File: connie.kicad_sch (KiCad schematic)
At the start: 143 parts, among them J1 Conn_01x03, J2 Conn_01x02, J3 Conn_01x02, J4 Conn_01x03, J5 Barrel_Jack_Switch, Q1 DTC143Z, Q2 DTC143Z, Q3 DTC143Z, Q4 DTC143Z, SW1 DIP_1188E, SW2 DIP_1188E, SW3 DIP_1188E, SW4 DIP_1188E, SW5 DIP_1188E, U1 emmc_bga153, U3 ES8388, U4 CS8676E, U5 74LVC1G02, U6 MAX803, U7 MAX803, U8 74LVC1G02, U9 TPS562200

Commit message: add c3 module
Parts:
- removed J1: Conn_01x03, Connector_PinHeader_2.54mm:PinHeader_1x03_P2.54mm_Vertical, symbol Connector_Generic:Conn_01x03
- added C100: 22u, Capacitor_SMD:C_1206_3216Metric, symbol Device:C
- added C101, C102: 0.1u, Capacitor_SMD:C_0603_1608Metric, symbol Device:C
- added J1: Conn_01x05, Connector_PinHeader_2.54mm:PinHeader_1x05_P2.54mm_Vertical, symbol Connector_Generic:Conn_01x05
- added R100, R101: 1k, Resistor_SMD:R_0603_1608Metric, symbol Device:R
- added R103, R104: 10k, Resistor_SMD:R_0603_1608Metric, symbol Device:R
- added U10: ESP32-C3-mini-1, Espressif:ESP32-C3-MINI-1, symbol connie-lib:c
- C15, C22, C23, C24: footprint Capacitor_SMD:C_0805_2012Metric -> Capacitor_SMD:C_0603_1608Metric
- R26, R27, R28, R31, R32, R33, R42, R43: value R -> 10k
- U2: value (none) -> ESP32_WROVER; footprint (none) -> Espressif:ESP32-WROVER-E_Thermal_Vias
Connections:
- net +3V3: now also R35.2, C100.2, C101.1, R103.1, R104.1, U10.3 (3V3); no longer R35.1
- net EN: now also C102.2, U10.8 (EN/CHIP_PU)
- net GND: now also C37.1, C100.1, C101.2, C102.1, J1.3 (Pin_3), J1.4 (Pin_4), U10.1 (GND), U10.11 (GND), U10.14 (GND), U10.2 (GND), U10.36 (GND); no longer C37.2
- net MODE: now also C37.2; no longer C37.1
- net OUTNL2: now also J3.1 (Pin_1); no longer J3.2 (Pin_2)
- net OUTNR2: now also J2.2 (Pin_2); no longer J2.1 (Pin_1)
- net OUTPL2: now also J3.2 (Pin_2); no longer J3.1 (Pin_1)
- net OUTPR2: now also J2.1 (Pin_1); no longer J2.2 (Pin_2)
- net PLAY: now also R35.1; no longer R35.2
- net RXD1: now also R101.1
- net TXD1: now also R100.1
- new net: R104.2, U10.22 (GPIO8)
- new net: R103.2, U10.5 (GPIO2/ADC1_CH2)
- new net: J1.5 (Pin_5), U10.23 (GPIO9)
- new net C3_RXD0: J1.2 (Pin_2), U10.30 (GPIO20/U0RXD)
- new net C3_RXD1: R100.2, U10.20 (GPIO6)
- new net C3_TXD0: J1.1 (Pin_1), U10.31 (GPIO21/U0TXD)
- new net C3_TXD1: R101.2, U10.21 (GPIO7)
- no-connect marks 18 -> 26
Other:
- moved on the sheet: C15, C22, C23, C24, C30, C31, C32, C33, C34, C35, C36, C37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

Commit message: prepare to rename refs
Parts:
- renumbered R2 to R1, R3 to R2, R4 to R3, R1 to R4
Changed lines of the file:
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@@
   (symbol (lib_id "Device:R") (at 21.59 160.02 90) (unit 1)
     (in_bom yes) (on_board yes)
-    (property "Reference" "R3" (id 0) (at 26.67 158.75 90))
+    (property "Reference" "R2" (id 0) (at 26.67 158.75 90))
     (property "Value" "33" (id 1) (at 21.59 160.02 90))
     (property "Footprint" "Resistor_SMD:R_0603_1608Metric" (id 2) (at 21.59 161.798 90)
@@
   (symbol (lib_id "Device:R") (at 21.59 165.1 90) (unit 1)
     (in_bom yes) (on_board yes)
-    (property "Reference" "R1" (id 0) (at 26.67 163.83 90))
+    (property "Reference" "R4" (id 0) (at 26.67 163.83 90))
     (property "Value" "33" (id 1) (at 21.59 165.1 90))
     (property "Footprint" "Resistor_SMD:R_0603_1608Metric" (id 2) (at 21.59 166.878 90)
@@
   (symbol (lib_id "Device:R") (at 21.59 157.48 90) (unit 1)
     (in_bom yes) (on_board yes)
-    (property "Reference" "R4" (id 0) (at 26.67 156.21 90))
+    (property "Reference" "R3" (id 0) (at 26.67 156.21 90))
     (property "Value" "33" (id 1) (at 21.59 157.48 90))
     (property "Footprint" "Resistor_SMD:R_0603_1608Metric" (id 2) (at 21.59 159.258 90)
@@
   (symbol (lib_id "Device:R") (at 21.59 162.56 90) (unit 1)
     (in_bom yes) (on_board yes)
-    (property "Reference" "R2" (id 0) (at 26.67 161.29 90))
+    (property "Reference" "R1" (id 0) (at 26.67 161.29 90))
     (property "Value" "33" (id 1) (at 21.59 162.56 90))
     (property "Footprint" "Resistor_SMD:R_0603_1608Metric" (id 2) (at 21.59 164.338 90)
@@
       (reference "Q4") (unit 1) (value "DTC143Z") (footprint "Package_TO_SOT_SMD:SOT-23")
     )
+    (path "/f95bf3a5-5302-41d3-a2db-2263542d0696"
+      (reference "R1") (unit 1) (value "33") (footprint "Resistor_SMD:R_0603_1608Metric")
+    )
+    (path "/94a054e2-bafe-477a-a6c6-a1ed40dff911"
+      (reference "R2") (unit 1) (value "33") (footprint "Resistor_SMD:R_0603_1608Metric")
+    )
+    (path "/ecc35952-8ff0-49f7-939a-ee69c7eb30f7"
+      (reference "R3") (unit 1) (value "33") (footprint "Resistor_SMD:R_0603_1608Metric")
+    )
     (path "/a95cdc4d-00a4-4bf0-80f3-df5d0747d5a0"
-      (reference "R1") (unit 1) (value "33") (footprint "Resistor_SMD:R_0603_1608Metric")
-    )
-    (path "/f95bf3a5-5302-41d3-a2db-2263542d0696"
-      (reference "R2") (unit 1) (value "33") (footprint "Resistor_SMD:R_0603_1608Metric")
-    )
-    (path "/94a054e2-bafe-477a-a6c6-a1ed40dff911"
-      (reference "R3") (unit 1) (value "33") (footprint "Resistor_SMD:R_0603_1608Metric")
-    )
-    (path "/ecc35952-8ff0-49f7-939a-ee69c7eb30f7"
       (reference "R4") (unit 1) (value "33") (footprint "Resistor_SMD:R_0603_1608Metric")
     )

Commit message: reannotate resistors
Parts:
- renumbered R8 to R10, R9 to R11, R15 to R12, R7 to R13, R10 to R14, R12 to R15, R100 to R16, R101 to R17, R14 to R18, R17 to R19, R16 to R20, R19 to R21, R20 to R22, R21 to R23, R23 to R24, R22 to R25, R24 to R26, R25 to R27, R103 to R28, R104 to R29, R28 to R30, R33 to R32, R27 to R33, R26 to R34, R32 to R35, R43 to R36, R42 to R37, R34 to R38, R35 to R39, R36 to R40, R30 to R41, R29 to R42, R44 to R43, R37 to R44, R38 to R45, R40 to R46, R39 to R47, R41 to R48, R48 to R49, R6 to R5, R45 to R50, R46 to R51, R47 to R52, R18 to R6, R13 to R7, R5 to R8, R11 to R9

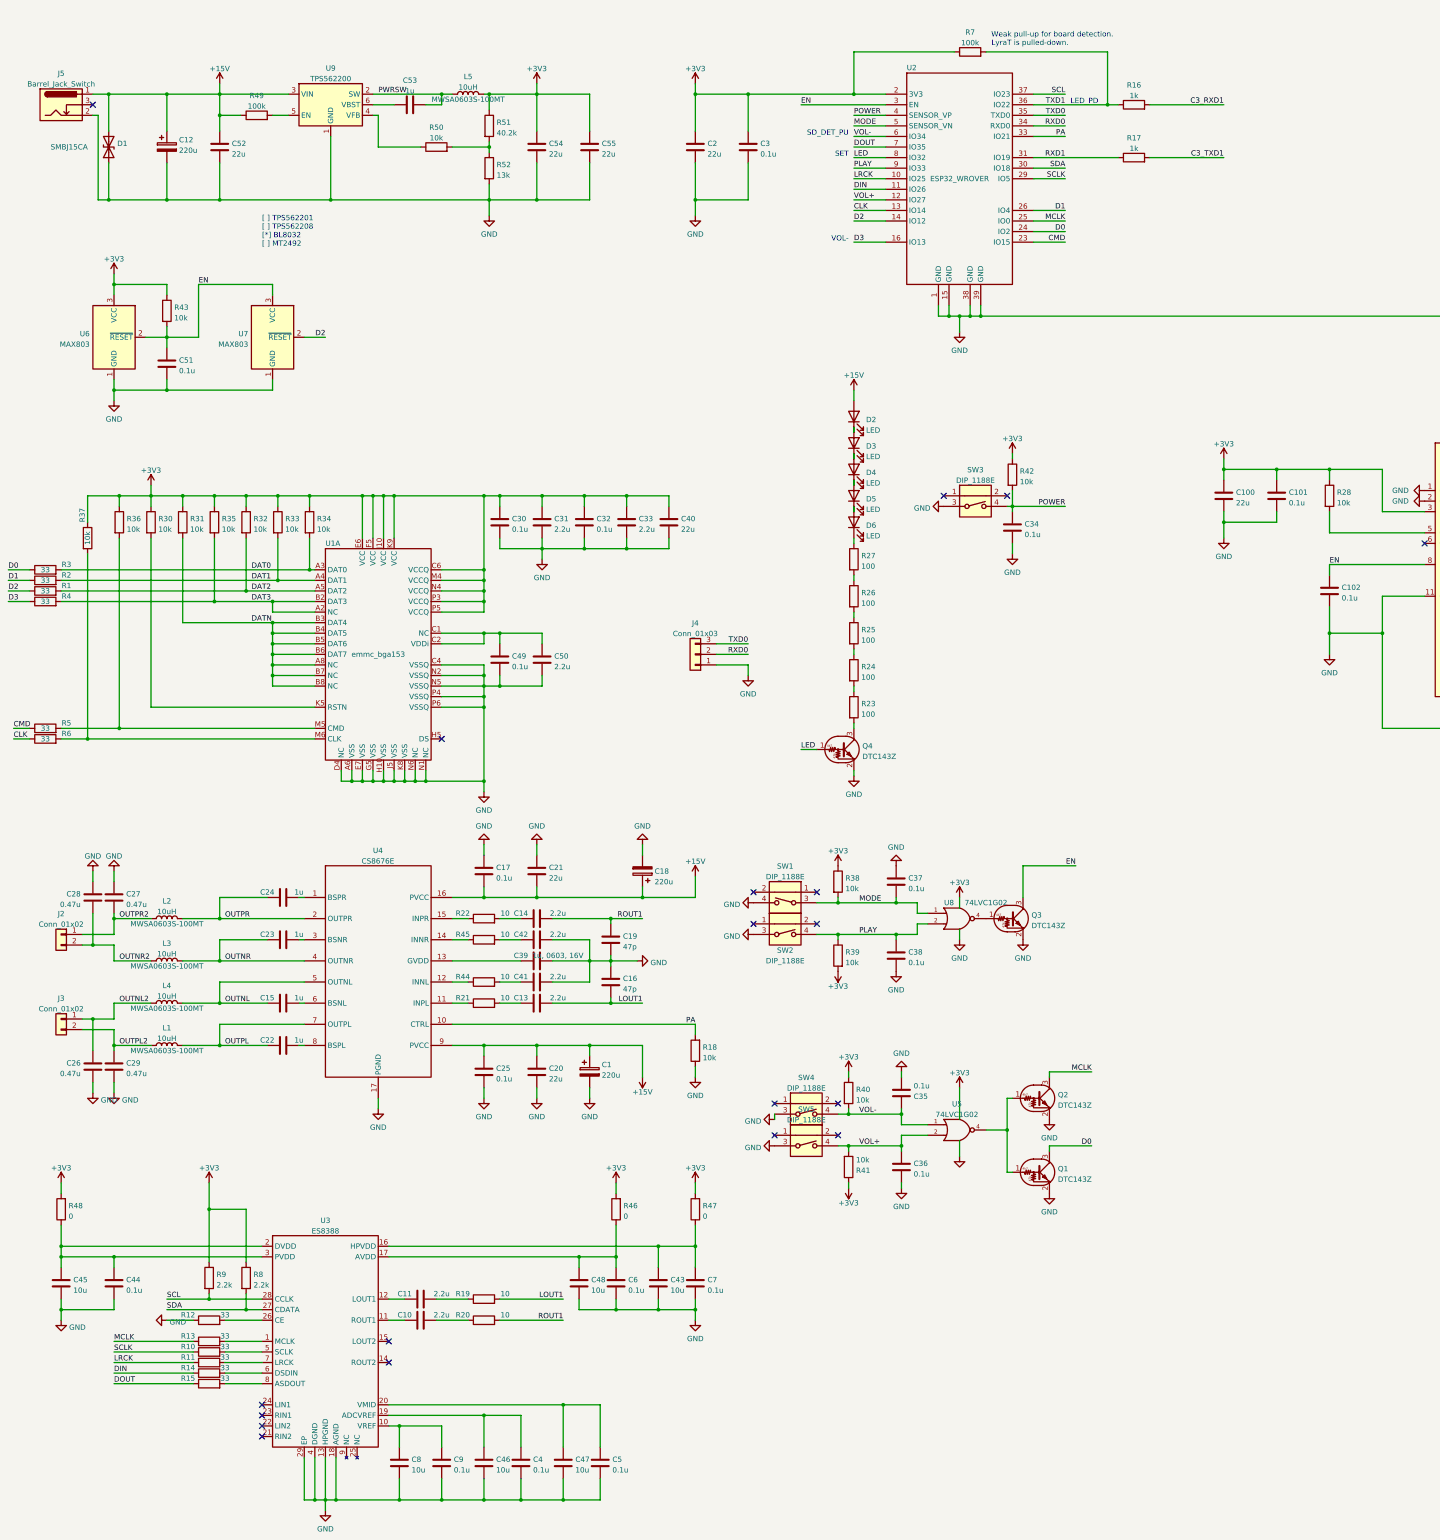
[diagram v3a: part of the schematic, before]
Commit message: reannotate caps
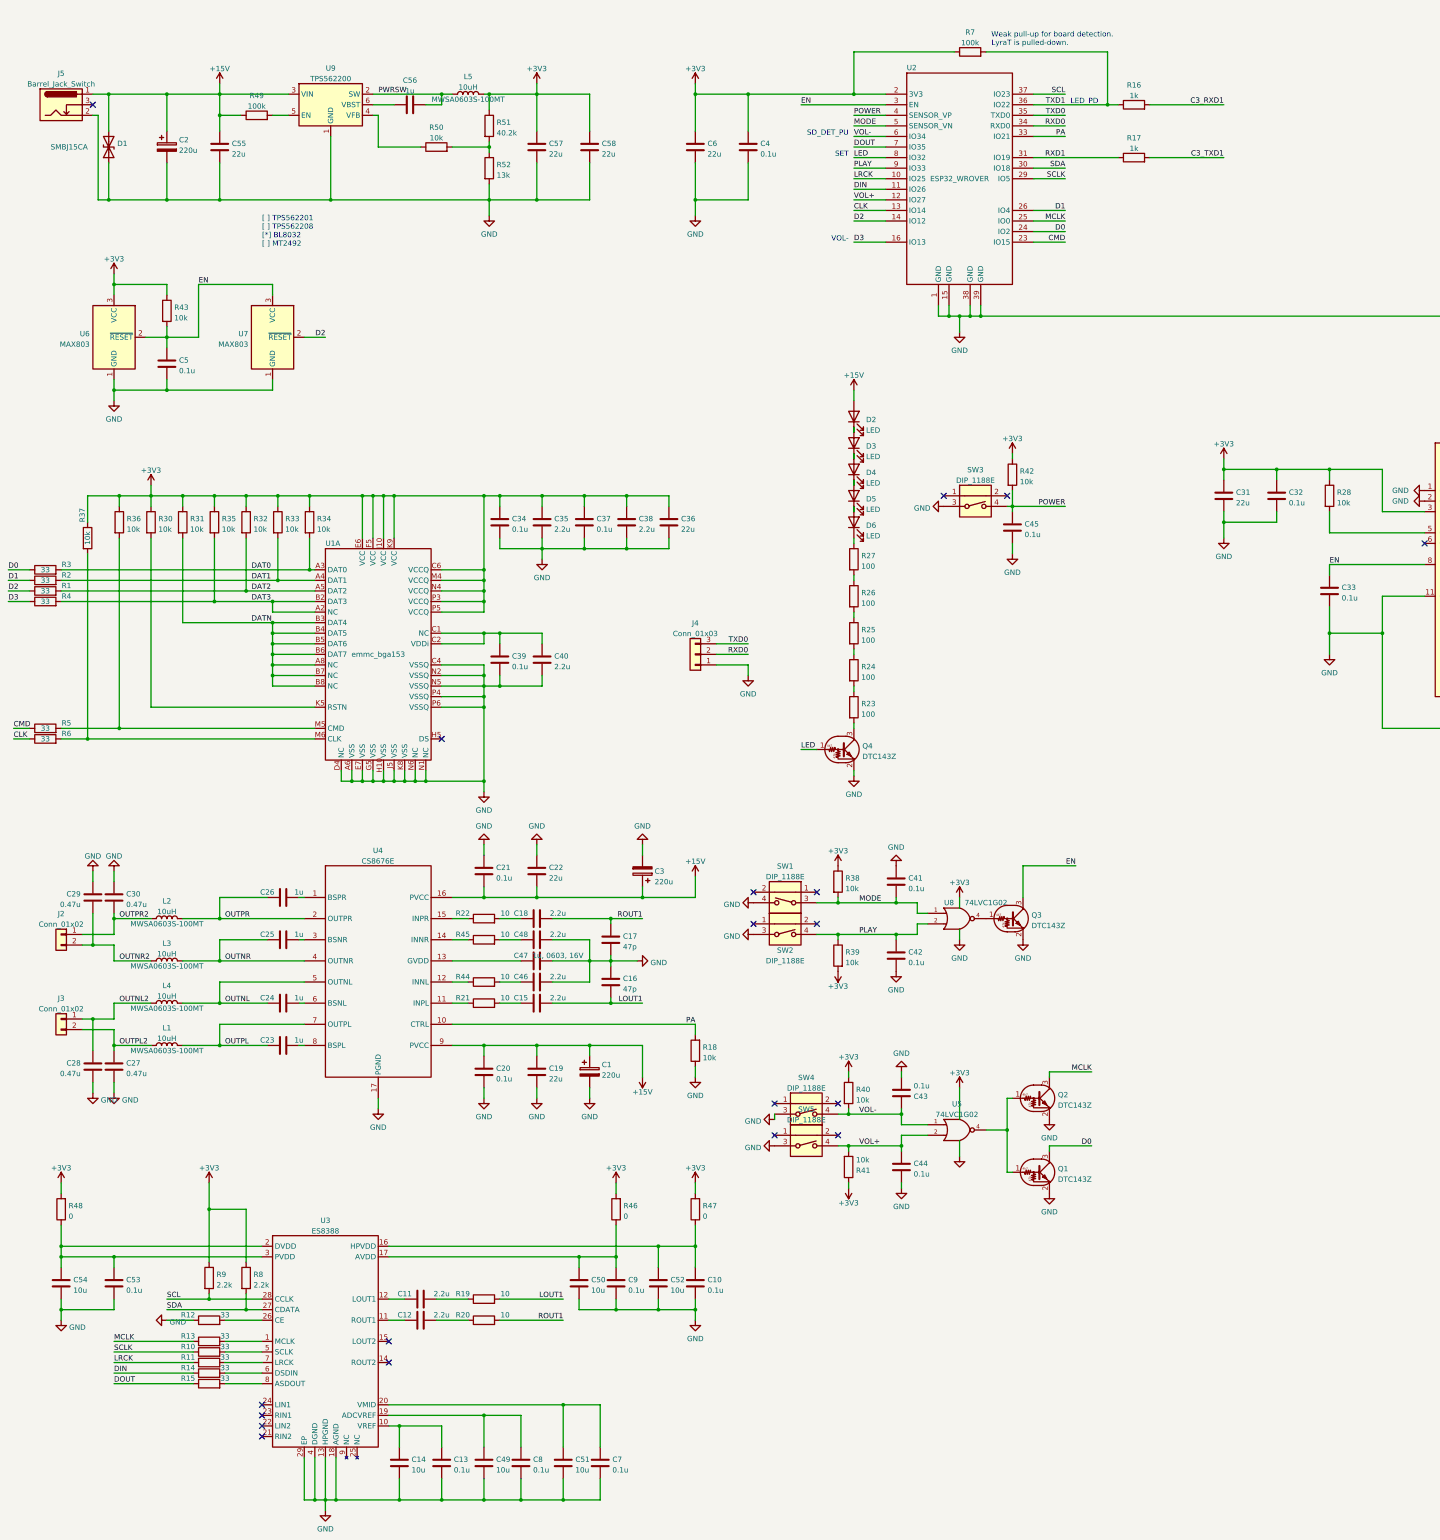
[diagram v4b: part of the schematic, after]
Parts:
- renumbered C7 to C10, C10 to C12, C9 to C13, C8 to C14, C13 to C15, C19 to C17, C14 to C18, C20 to C19, C12 to C2, C25 to C20, C17 to C21, C21 to C22, C22 to C23, C15 to C24, C23 to C25, C24 to C26, C29 to C27, C26 to C28, C28 to C29, C18 to C3, C27 to C30, C100 to C31, C101 to C32, C102 to C33, C30 to C34, C31 to C35, C40 to C36, C32 to C37, C33 to C38, C49 to C39, C3 to C4, C50 to C40, C37 to C41, C38 to C42, C35 to C43, C36 to C44, C34 to C45, C41 to C46, C39 to C47, C42 to C48, C46 to C49, C51 to C5, C48 to C50, C47 to C51, C43 to C52, C44 to C53, C45 to C54, C52 to C55, C53 to C56, C54 to C57, C55 to C58, C2 to C6, C5 to C7, C4 to C8, C6 to C9

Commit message: prepare for manufacturing
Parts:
- removed U10: ESP32-C3-mini-1, Espressif:ESP32-C3-MINI-1, symbol connie-lib:c
- added FID1, FID2, FID3, FID4, FID5, FID6: (no value), symbol Mechanical:Fiducial
- added TP1, TP10, TP11, TP12, TP13, TP2, TP3, TP4, TP5, TP6, TP7: (no value), symbol Connector:TestPoint
- added U5: (no value), symbol connie-lib:ESP32-C3-MINI-1
- C1, C2, C3: value 220u -> (none); footprint Capacitor_SMD:CP_Elec_8x10.5 -> (none)
- C10, C13, C32, C33, C34, C37, C39, C4, C41, C42, C43, C44, C45, C5, C53, C7, C8, C9: value 0.1u -> (none); footprint Capacitor_SMD:C_0603_1608Metric -> (none)
- C11, C12, C15, C18, C35, C38, C40, C46, C48: value 2.2u -> (none); footprint Capacitor_SMD:C_0603_1608Metric -> (none)
- C14, C49, C50, C51, C52, C54: value 10u -> (none); footprint Capacitor_SMD:C_0805_2012Metric -> (none)
- C16, C17: value 47p -> (none); footprint Capacitor_SMD:C_0603_1608Metric -> (none)
- C19, C22, C31, C36, C55, C57, C58, C6: value 22u -> (none); footprint Capacitor_SMD:C_1206_3216Metric -> (none)
- C20, C21: value 0.1u -> (none); footprint Capacitor_SMD:C_0805_2012Metric -> (none)
- C23, C24, C25, C26, C56: value 1u -> (none); footprint Capacitor_SMD:C_0603_1608Metric -> (none)
- C27, C28, C29, C30: value 0.47u -> (none); footprint Capacitor_SMD:C_0805_2012Metric -> (none)
- C47: value 1u, 0603, 16V -> (none); footprint Capacitor_SMD:C_0603_1608Metric -> (none)
- D1: value SMBJ15CA -> (none); footprint Diode_SMD:D_SMB -> (none)
- D2, D3, D4, D5, D6: value LED -> (none); footprint LED_SMD:LED_0603_1608Metric -> (none)
- H1, H2, H3, H5: value MountingHole -> (none); footprint Library:MountingHole_2.8mm_M2.5 -> (none)
- H4, H6: value MountingHole -> (none); footprint Library:MountingHole_1.7mm -> (none)
- J1: renamed from J3; value Conn_01x02 -> (none); footprint Connector_JST:JST_PH_B2B-PH-K_1x02_P2.00mm_Vertical -> (none)
- J2: value Conn_01x02 -> (none); footprint Connector_JST:JST_PH_B2B-PH-K_1x02_P2.00mm_Vertical -> (none)
- J3: renamed from J1; value Conn_01x05 -> (none); footprint Connector_PinHeader_2.54mm:PinHeader_1x05_P2.54mm_Vertical -> (none)
- J4: value Conn_01x03 -> (none); footprint Connector_PinHeader_2.54mm:PinHeader_1x03_P2.54mm_Vertical -> (none)
- J5: value Barrel_Jack_Switch -> (none); footprint Library:69410X402002 -> (none)
- L1, L3, L5: value 10uH -> (none); footprint Library:Sunlord_MWSA0603_6.6x7.1_H3.0 -> (none)
- L2: renamed from L4; value 10uH -> (none); footprint Library:Sunlord_MWSA0603_6.6x7.1_H3.0 -> (none)
- L4: renamed from L2; value 10uH -> (none); footprint Library:Sunlord_MWSA0603_6.6x7.1_H3.0 -> (none)
- Q1: renamed from Q4; value DTC143Z -> (none); footprint Package_TO_SOT_SMD:SOT-23 -> (none)
- Q2: renamed from Q1; value DTC143Z -> (none); footprint Package_TO_SOT_SMD:SOT-23 -> (none)
- Q3: renamed from Q2; value DTC143Z -> (none); footprint Package_TO_SOT_SMD:SOT-23 -> (none)
- Q4: renamed from Q3; value DTC143Z -> (none); footprint Package_TO_SOT_SMD:SOT-23 -> (none)
- R1, R10, R11, R12, R13, R14, R15, R2, R3, R4, R5, R6: value 33 -> (none); footprint Resistor_SMD:R_0603_1608Metric -> (none)
- R16, R17: value 1k -> (none); footprint Resistor_SMD:R_0603_1608Metric -> (none)
- R18, R28, R29, R30, R31, R32, R33, R34, R35, R36, R37, R38, R39, R40, R41, R42, R43, R50: value 10k -> (none); footprint Resistor_SMD:R_0603_1608Metric -> (none)
- R19, R20, R21, R22, R44, R45: value 10 -> (none); footprint Resistor_SMD:R_0603_1608Metric -> (none)
- R23, R24, R25, R26, R27: value 100 -> (none); footprint Resistor_SMD:R_0603_1608Metric -> (none)
- R46, R47, R48: value 0 -> (none); footprint Resistor_SMD:R_0603_1608Metric -> (none)
- R49, R7: value 100k -> (none); footprint Resistor_SMD:R_0603_1608Metric -> (none)
- R51: value 40.2k -> (none); footprint Resistor_SMD:R_0603_1608Metric -> (none)
- R52: value 13k -> (none); footprint Resistor_SMD:R_0603_1608Metric -> (none)
- R8, R9: value 2.2k -> (none); footprint Resistor_SMD:R_0603_1608Metric -> (none)
- SW1: renamed from SW5; value DIP_1188E -> (none); footprint Library:DIP_1188E -> (none); symbol connie-lib:DIP_1188E -> Connie:DIP1188E
- SW2: renamed from SW4; value DIP_1188E -> (none); footprint Library:DIP_1188E -> (none); symbol connie-lib:DIP_1188E -> Connie:DIP1188E
- SW3: value DIP_1188E -> (none); footprint Library:DIP_1188E -> (none); symbol connie-lib:DIP_1188E -> Connie:DIP1188E
- SW4: renamed from SW2; value DIP_1188E -> (none); footprint Library:DIP_1188E -> (none); symbol connie-lib:DIP_1188E -> Connie:DIP1188E
- SW5: renamed from SW1; value DIP_1188E -> (none); footprint Library:DIP_1188E -> (none); symbol connie-lib:DIP_1188E -> Connie:DIP1188E
- U1: renamed from U2; value ESP32_WROVER -> (none); footprint Espressif:ESP32-WROVER-E_Thermal_Vias -> (none); symbol connie-lib:ESP32_WROVER -> Connie:ESP32-WROVER-E
- U10: renamed from U9; value TPS562200 -> (none); footprint Package_TO_SOT_SMD:SOT-23-6 -> (none); symbol Regulator_Switching:TPS562200 -> Connie:TPS562200
- U2: renamed from U1; value emmc_bga153 -> (none); footprint Library:EMMC_BGA153 -> (none); symbol connie-lib:emmc_bga153 -> Connie:EMMC(BGA153)
- U3: value ES8388 -> (none); footprint Library:QFN-28_EP_4x4_Pitch0.45mm -> (none); symbol connie-lib:ES8388 -> Connie:ES8388
- U4: value CS8676E -> (none); footprint Library:CS8676E_SOP-16_3.9x9.9mm_P1.27mm -> (none); symbol connie-lib:CS8676E -> Connie:CS8676E
- U6: renamed from U5; value 74LVC1G02 -> (none); footprint Package_TO_SOT_SMD:SOT-23-5 -> (none)
- U7: value MAX803 -> (none); footprint Package_TO_SOT_SMD:SOT-23 -> (none)
- U8: value 74LVC1G02 -> (none); footprint Package_TO_SOT_SMD:SOT-23-5 -> (none)
- U9: renamed from U6; value MAX803 -> (none); footprint Package_TO_SOT_SMD:SOT-23 -> (none)
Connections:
- net +15V: now also R23.1, R49.2; no longer D2.2 (A), R49.1
- net +3V3: now also U5.3 (3V3)
- net C3_RXD0: now also U5.30 (IO22)
- net C3_RXD1: now also U5.20 (IO6)
- net C3_TXD0: now also U5.31 (IO21)
- net C3_TXD1: now also U5.21 (IO7)
- net D0: now also TP5.1
- net D2: now also TP7.1
- net EN: now also U5.8 (EN)
- net GND: now also C43.1, TP3.1, TP6.1, U5.1 (GND), U5.11 (GND), U5.14 (GND), U5.2 (GND), U5.36 (GND); no longer C43.2
- net MCLK: now also TP4.1
- net MODE: now also U6.1, U8.2; no longer U8.1
- net OUTNL2: now also TP11.1
- net OUTNR2: now also TP13.1
- net OUTPL2: now also TP10.1
- net OUTPR2: now also TP12.1
- net PLAY: now also U6.2; no longer U8.2
- net POWER: now also U8.1
- net RXD0: now also TP2.1
- net TXD0: now also TP1.1
- net VOL+: no longer U6.2
- net VOL-: now also C43.2; no longer C43.1, U6.1
- net at R29.2: now also U5.22 (IO8)
- net at R28.2: now also U5.5 (IO2)
- net C3_IO9: now reaches J3.5 (Pin_5)
- net C3_IO9: now also U5.23 (IO9)
- net at U10.5 (EN): now also R49.1; no longer R49.2
- net at R24.2: now also Q1.3 (C); no longer R23.1
- net at R23.2: now also D2.2 (A); no longer Q1.3 (C)
- no-connect marks 26 -> 16
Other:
- moved on the sheet: C1, C10, C11, C12, C13, C14, C15, C16, C17, C18, C19, C2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
